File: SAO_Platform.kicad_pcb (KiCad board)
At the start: 2 copper layers, 150 x 50 mm, 18 parts, among them J1 KH_Type-C-16P, J10 Conn_02x03_Counter_Clockwise, J11 AVR-ISP-6, J2 Conn_02x03_Counter_Clockwise, J3 Conn_02x03_Counter_Clockwise, J4 Conn_02x03_Counter_Clockwise, J5 Conn_02x03_Counter_Clockwise, J6 Conn_02x03_Counter_Clockwise, J7 Conn_02x03_Counter_Clockwise, J8 Conn_02x03_Counter_Clockwise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

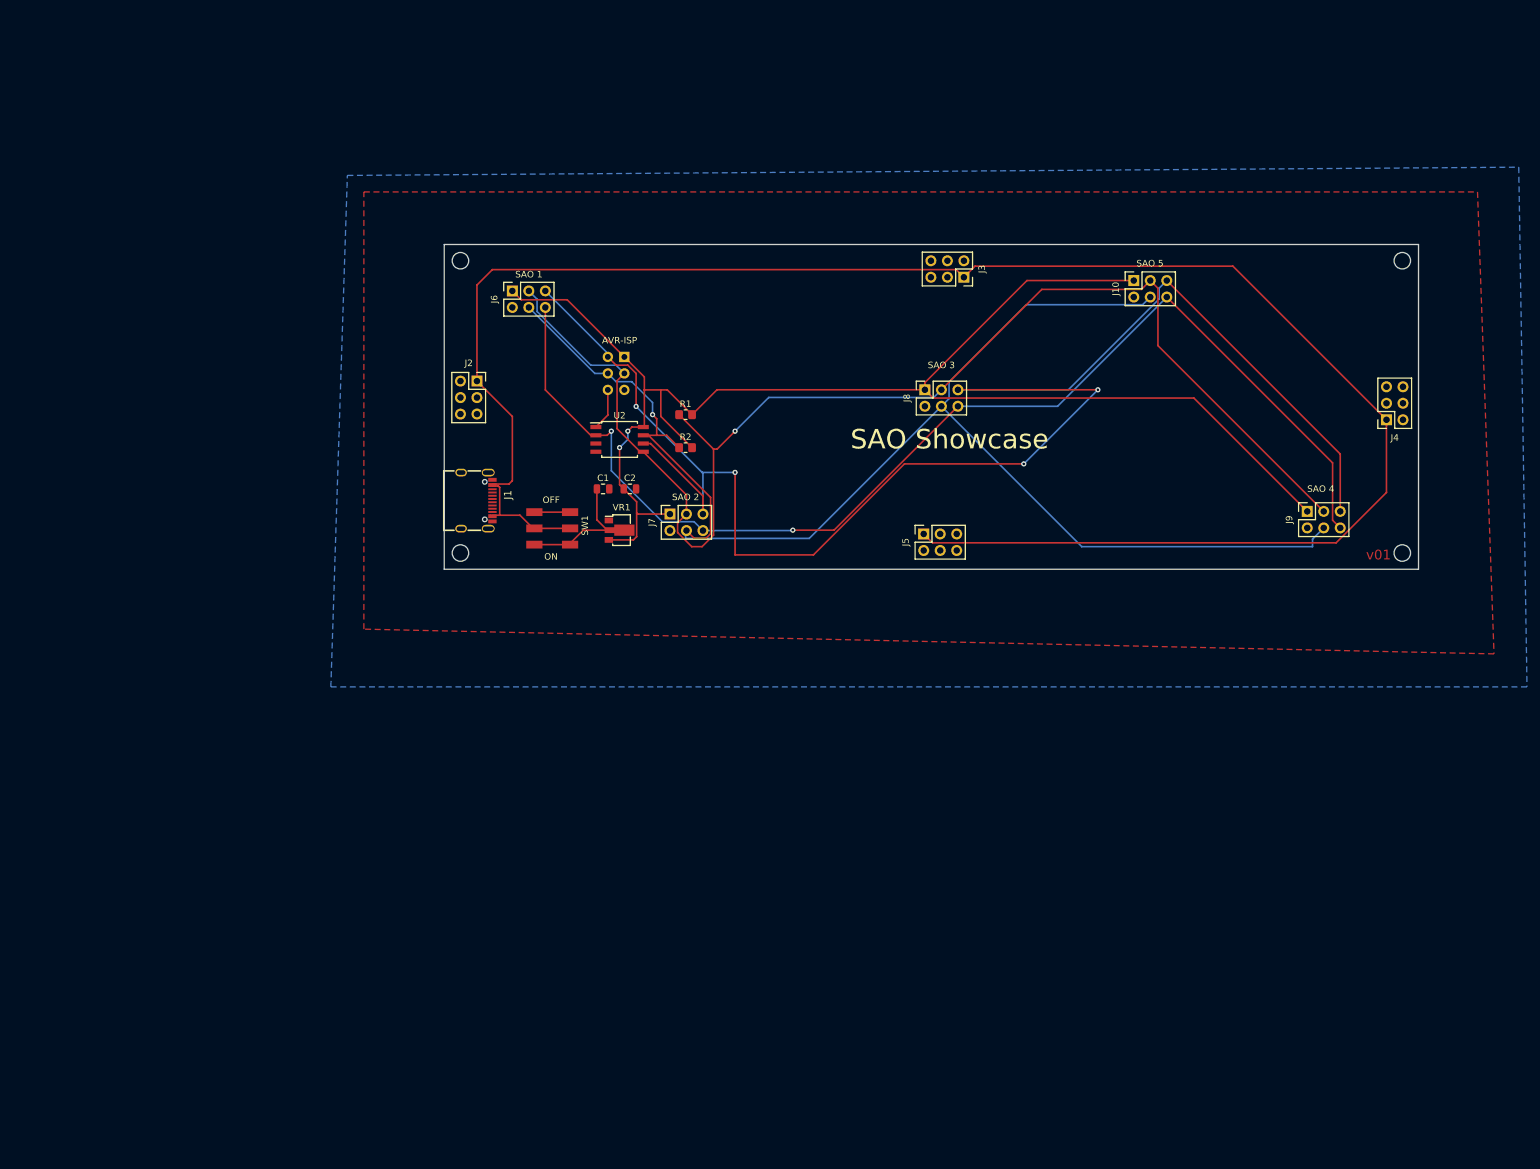
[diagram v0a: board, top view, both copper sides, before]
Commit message: reference runway images for the SAO platform
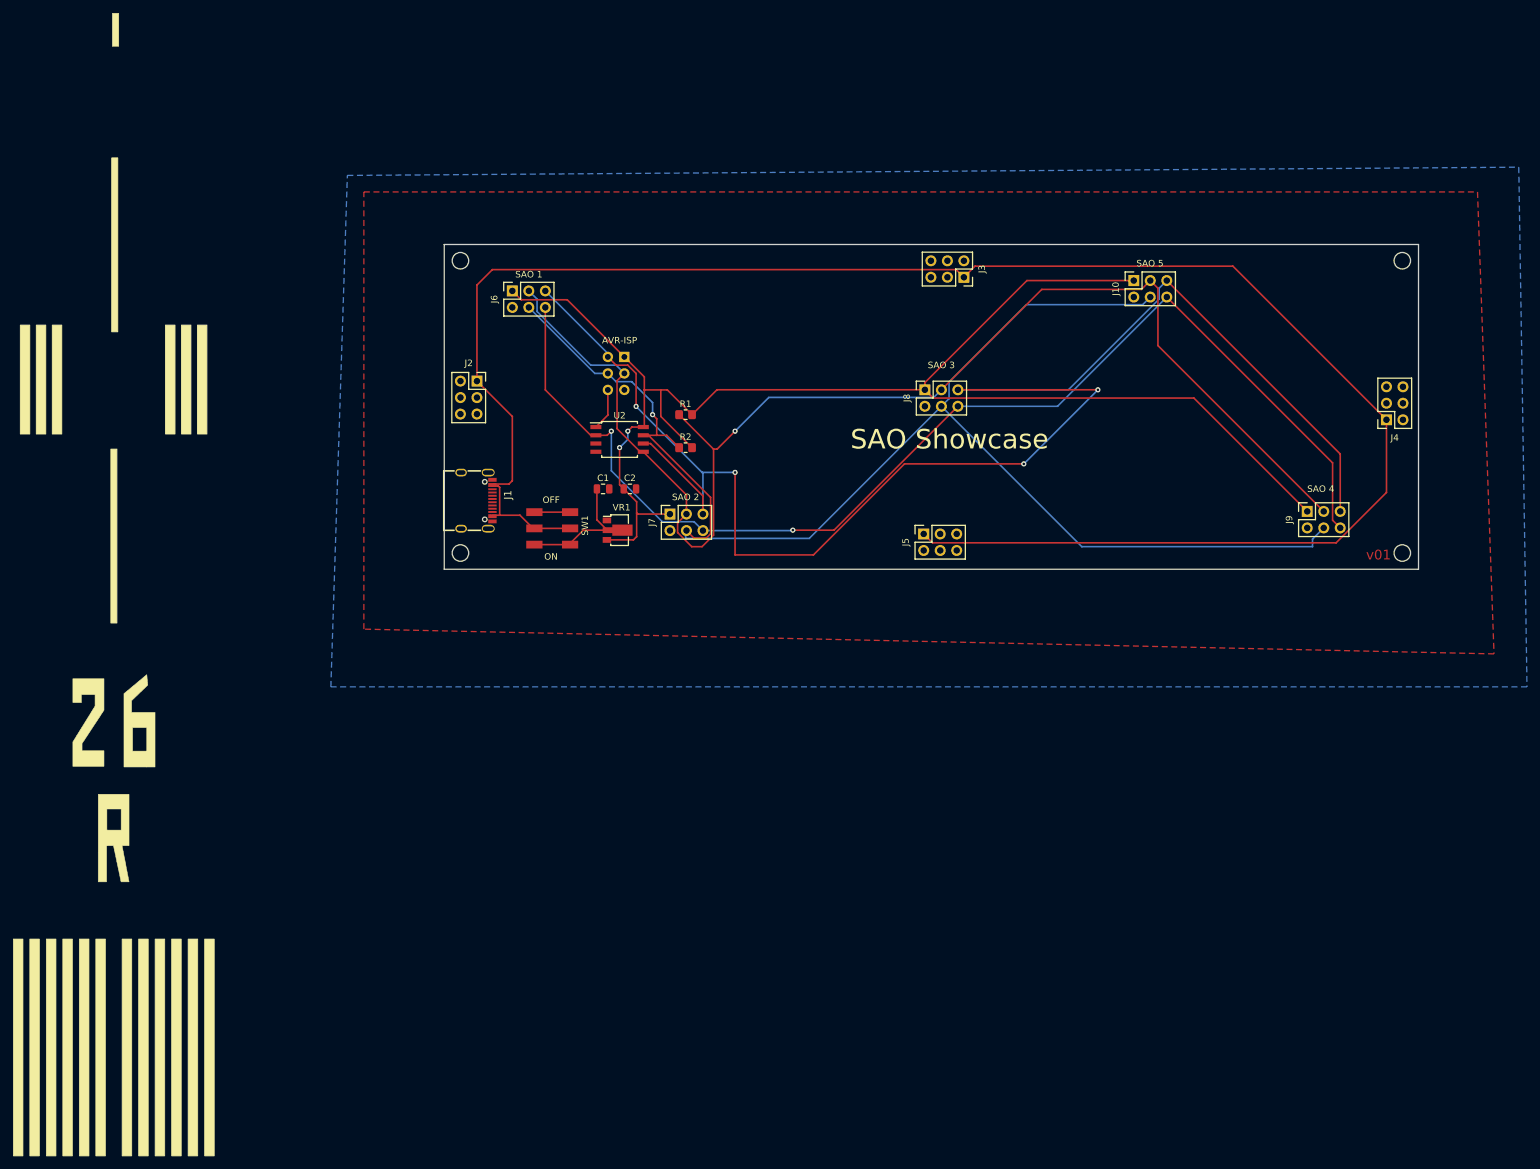
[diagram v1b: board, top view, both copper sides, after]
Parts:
- added svg2mod: G***, images:26R, F.Cu at (49.0, 103.5)
